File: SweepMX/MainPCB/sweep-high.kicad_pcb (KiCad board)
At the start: 2 copper layers, 229.5 x 95.2 mm, 61 parts, among them J1 AudioJack4dpb, J2 AudioJack4dpb, SW10 SW_Push, SW10_r1 SW_Push, SW11 SW_Push, SW11_r1 SW_Push, SW12 SW_Push, SW12_r1 SW_Push, SW14 SW_Push, SW14_r1 SW_Push, SW15 SW_Push, SW15_r1 SW_Push, SW16 SW_Push, SW16_r1 SW_Push, SW17 SW_Push, SW17_r1 SW_Push, SW18 SW_Push, SW18_r1 SW_Push, SW2 SW_Push, SW20 SW_Push, SW20_r1 SW_Push, SW21 SW_Push, SW21_r1 SW_Push, SW2_r1 SW_Push, SW3 SW_Push, SW3_r1 SW_Push, SW4 SW_Push, SW4_r1 SW_Push, SW5 SW_Push, SW5_r1 SW_Push, SW6 SW_Push, SW6_r1 SW_Push, SW8 SW_Push, SW8_r1 SW_Push, SW9 SW_Push, SW9_r1 SW_Push, U1 ProMicro-kbd, U2 ProMicro-kbd

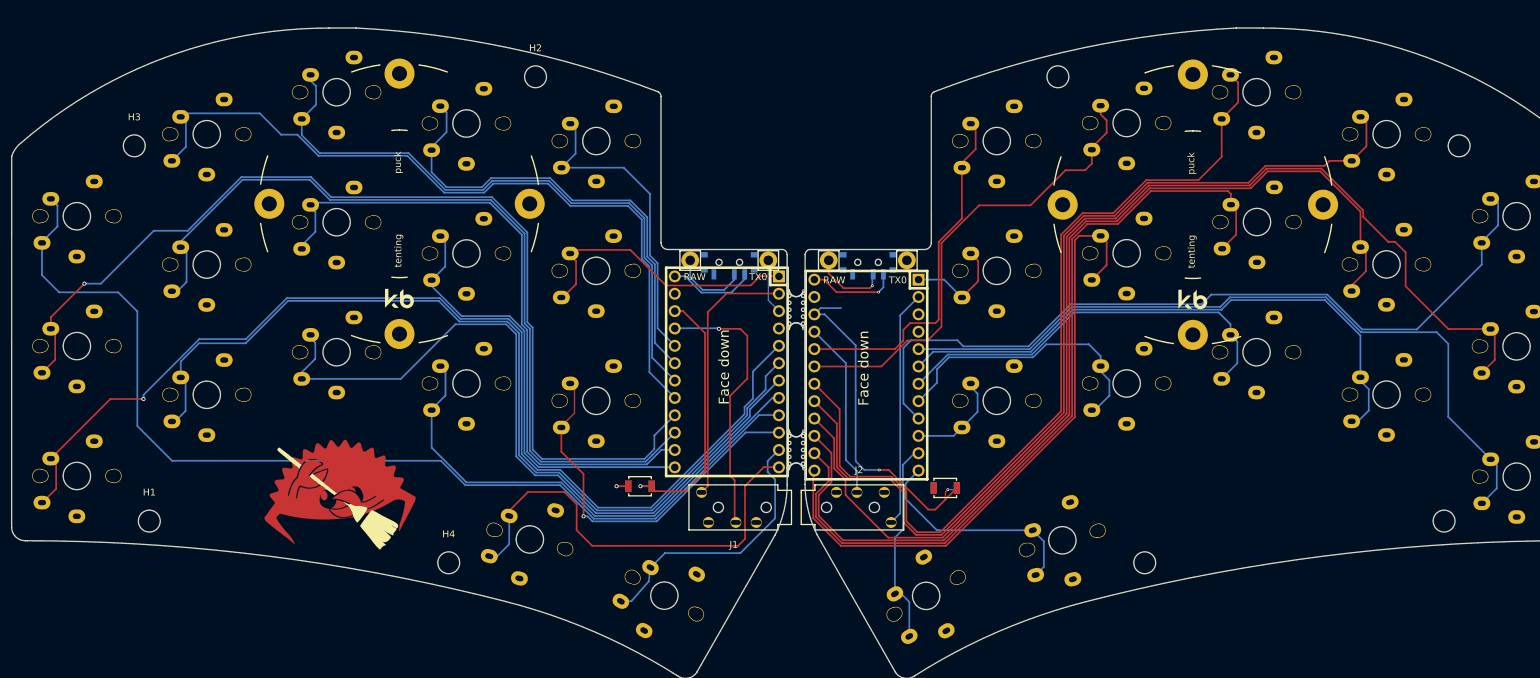
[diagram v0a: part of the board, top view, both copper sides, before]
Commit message: smol alignment fix
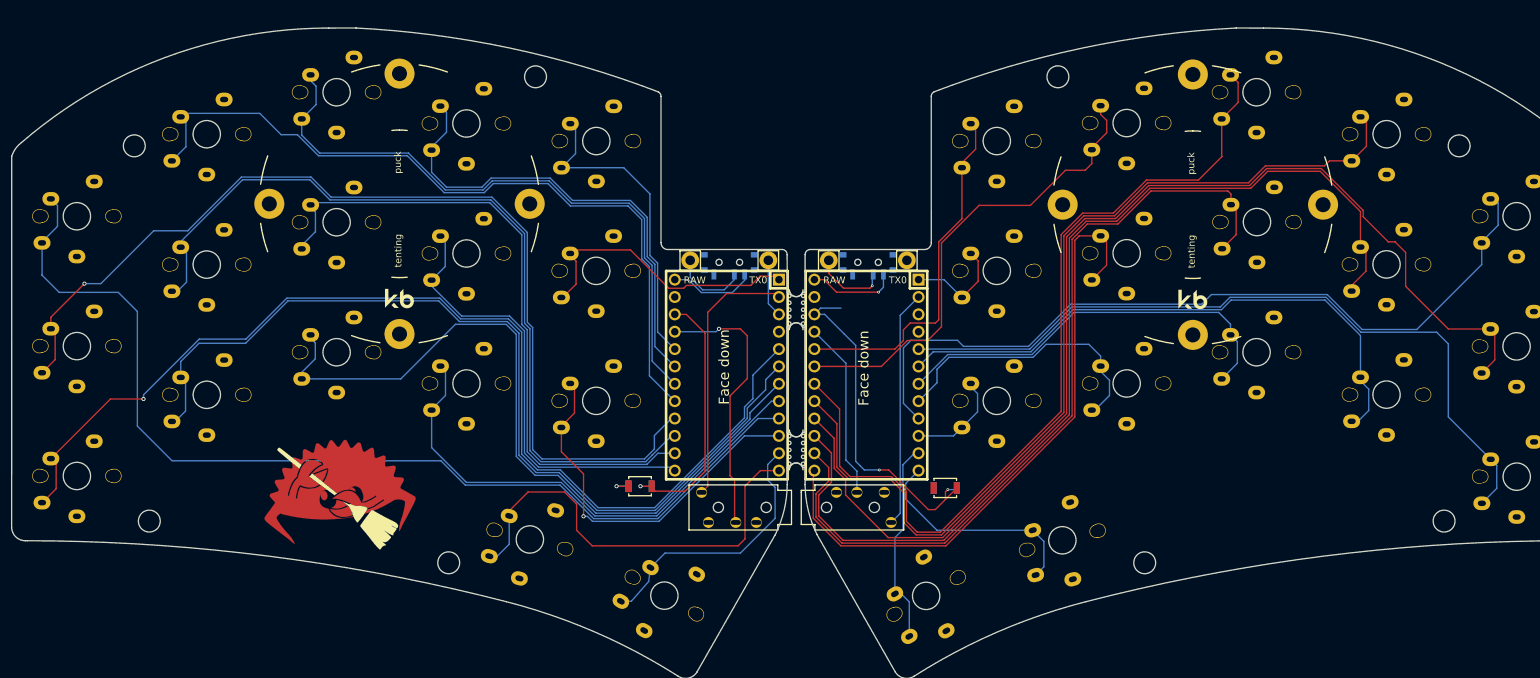
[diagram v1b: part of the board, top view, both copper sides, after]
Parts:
- moved U1 0.47 mm to (140.1, 100.2)
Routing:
- net gnd: track 11.5 -> 12.0 mm
- net Switch3: track 91.8 -> 92.3 mm
- net Switch5: track 45.8 -> 46.3 mm
- net Switch4: track 69.3 -> 69.8 mm
- net Switch2: track 110.9 -> 111.4 mm
